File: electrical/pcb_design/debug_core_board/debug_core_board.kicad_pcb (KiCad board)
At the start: 4 copper layers, 70.1 x 65.2 mm, 18 parts, among them J17 STLINK_TagConnect_6, U1 BMI323, U2 BMI323, U3 TCAN330, U4 STM32L452CEU6

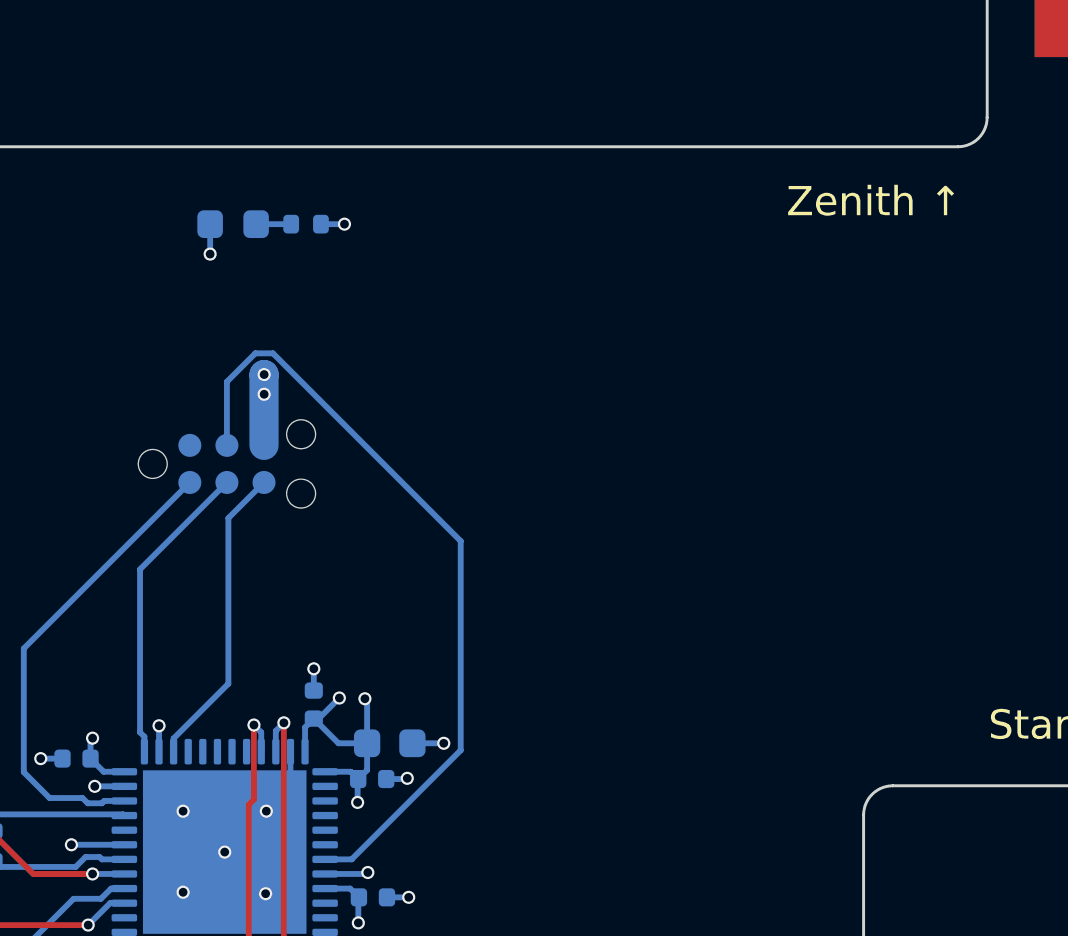
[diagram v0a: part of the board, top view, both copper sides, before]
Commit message: Added fake solar power generation
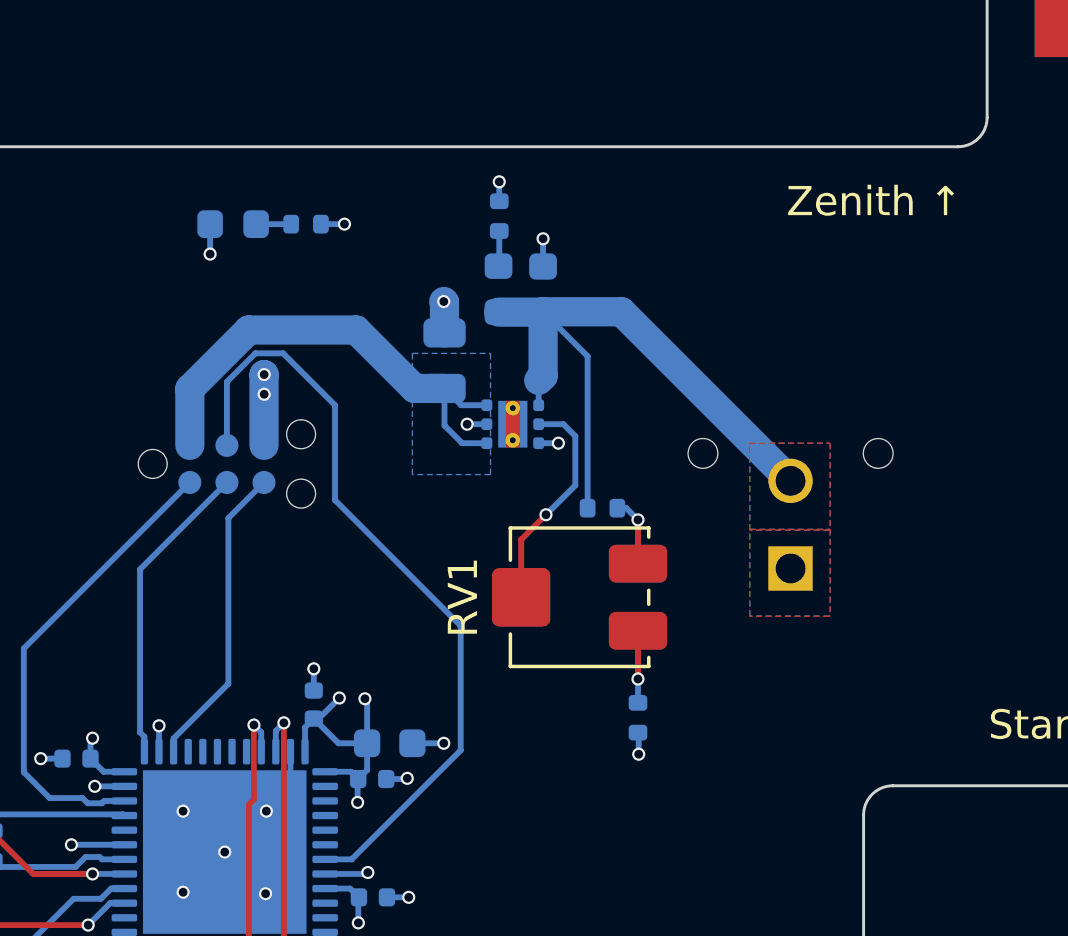
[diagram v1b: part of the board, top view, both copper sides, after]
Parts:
- added C7: 1u, Capacitor_SMD:C_0805_2012Metric, B.Cu at (150.4, 76.7)
- added C8: 10u, footprints:Nondescript_C_0603_1608Metric, B.Cu at (153.8, 74.2)
- added D2: Blue LED, LED_SMD:LED_0603_1608Metric, B.Cu at (152.3, 74.2)
- added J1: Molex_430450212, footprints:Molex_430450212, B.Cu at (162.3, 83.8)
- added R4: 68, Resistor_SMD:R_0402_1005Metric, B.Cu at (152.3, 71.7)
- added R5: 36k, Resistor_SMD:R_0402_1005Metric, B.Cu at (155.8, 81.7)
- added R6: 36k, Resistor_SMD:R_0402_1005Metric, B.Cu at (157.1, 88.9)
- added RV1: 500k, Potentiometer_SMD:Potentiometer_Bourns_3314J_Vertical, F.Cu at (155.1, 84.8)
- added U5: TLV76701DRVx, Package_SON:WSON-6-1EP_2x2mm_P0.65mm_EP1x1.6mm_ThermalVias, B.Cu at (152.8, 78.8)
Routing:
- net Net-(D2-A): track 0.00 -> 23.1 mm
- net VCC: track 0.00 -> 17.0 mm
- net Net-(U5-FB): track 0.00 -> 7.71 mm, vias 0 -> 1
- net GND: track 24.0 -> 28.8 mm, vias 24 -> 30
- net Net-(R6-Pad1): track 0.00 -> 2.46 mm, vias 0 -> 1
- net Net-(R5-Pad2): track 0.00 -> 2.37 mm, vias 0 -> 1
- net Net-(D2-K): track 0.00 -> 1.18 mm
- added copper zone on B.Cu, net GND
- added copper zone on F.Cu, net GND
- added copper zone on In1.Cu, net GND
- added copper zone on B.Cu, net Net-(D2-A)
- added copper zone on F.Cu, net Net-(D2-A)
- added copper zone on In1.Cu, net Net-(D2-A)
- added copper zone on In2.Cu, net Net-(D2-A)
- added copper zone on B.Cu, net VCC
